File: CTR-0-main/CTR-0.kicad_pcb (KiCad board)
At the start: 2 copper layers, 21 x 51 mm, 38 parts, among them J1 USB_C_Receptacle_USB2.0_14P, J2 Conn_01x20, J3 Conn_01x20, J4 Conn_01x03, SW1 SW_Push, SW2 SW_Push, U1 RP2040, U2 NCP1117-3.3_SOT223, U3 W25Q128JVS, U4 TVS1400DRV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

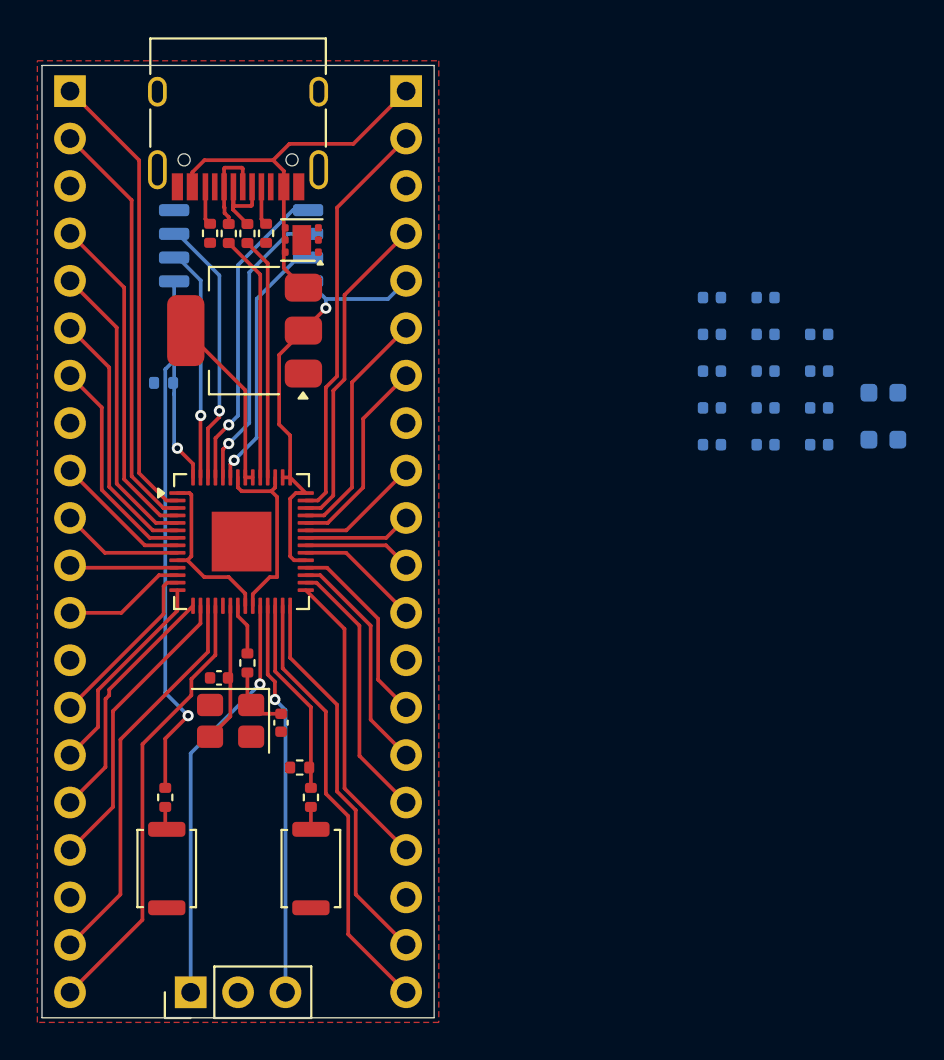
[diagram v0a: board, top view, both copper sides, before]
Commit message: fixes+final route
+decoupling capacitors
-clearance errors
-library footprint errors
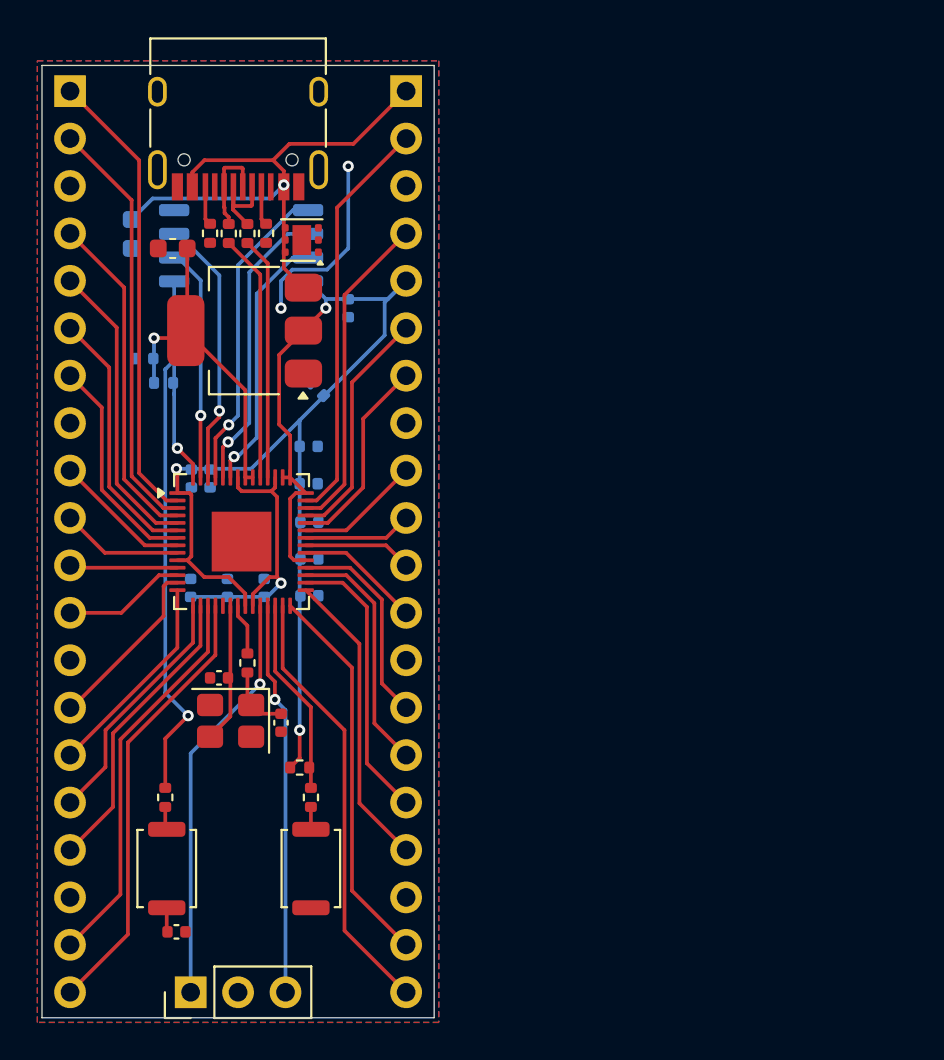
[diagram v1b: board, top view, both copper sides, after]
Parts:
- C2, C5: moved to F.Cu
- moved C1 41.7 mm to (184.8, 79.0), turned to -90 degrees
- moved C2 38.8 mm to (187.0, 79.8), turned to 180 degrees
- moved C5 38.8 mm to (187.2, 116.4), turned to 180 degrees
- moved C17 35.6 mm to (188.0, 98.0), turned to 90 degrees
- moved C14 33.4 mm to (185.5, 85.7), turned to 180 degrees
- moved C16 33.1 mm to (189.9, 98.0), turned to 90 degrees
- moved C13 30.7 mm to (189.0, 92.1), turned to -90 degrees
- moved C15 30.7 mm to (191.9, 98.0), turned to 90 degrees
- moved C8 28.9 mm to (188.0, 92.1), turned to -90 degrees
- moved C18 27.0 mm to (194.7, 87.3), turned to -45 degrees
- moved C10 25.7 mm to (194.3, 98.4)
- moved C11 25.7 mm to (194.3, 96.4)
- moved C12 25.7 mm to (194.3, 94.5)
- moved C6 22.0 mm to (194.3, 92.4)
- moved C7 22.0 mm to (194.3, 90.4)
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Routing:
- net +3V3: track 42.3 -> 88.6 mm, vias 1 -> 4
- net (no net): track 0.00 -> 10.4 mm, vias 0 -> 2
- net +5V: track 21.5 -> 30.5 mm, vias 0 -> 1
- net +1V1: track 10.3 -> 15.8 mm, vias 0 -> 1
- net Net-(C5-Pad2): track 0.00 -> 1.31 mm
- net /GPIO20: track 12.3 -> 13.1 mm
- net /GPIO19: track 14.3 -> 15.2 mm
- net /GPIO21: track 10.4 -> 11.1 mm
- added copper zone on B.Cu, net GND
